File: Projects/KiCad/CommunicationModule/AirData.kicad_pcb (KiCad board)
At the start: 2 copper layers, 110 x 95 mm, 36 parts, among them J1 Conn_01x08, SW1 SW_DIP_x02, U1 MCP2562-E-P, U2 MCP2515-I/P, U3 NJM7805SDL1, U4 ABX00012, Y1 8MHz

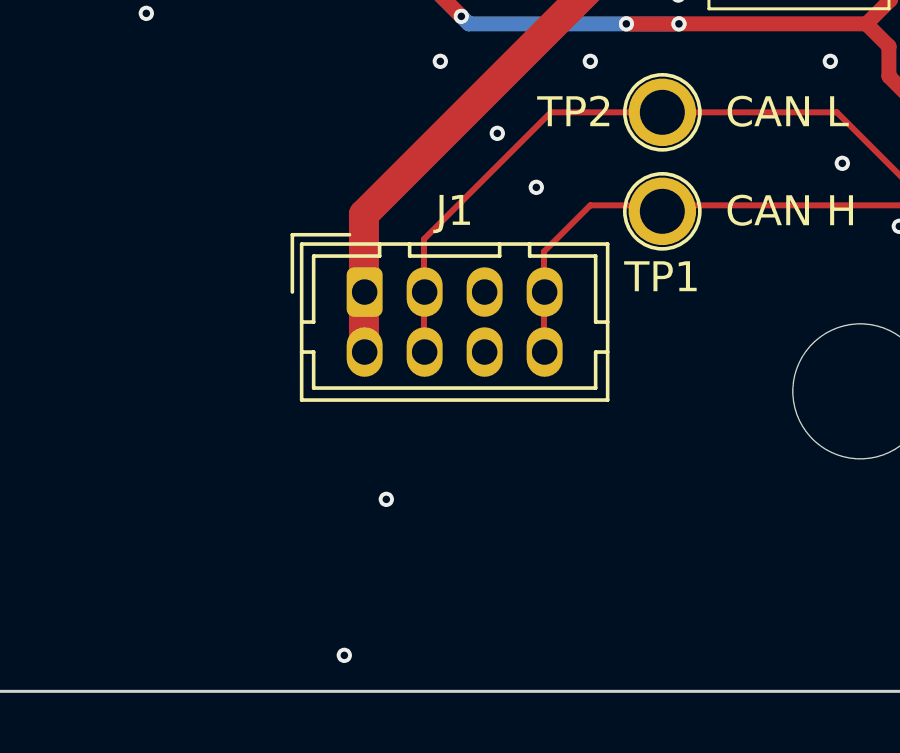
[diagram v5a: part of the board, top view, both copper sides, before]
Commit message: STEPファイルを再生成
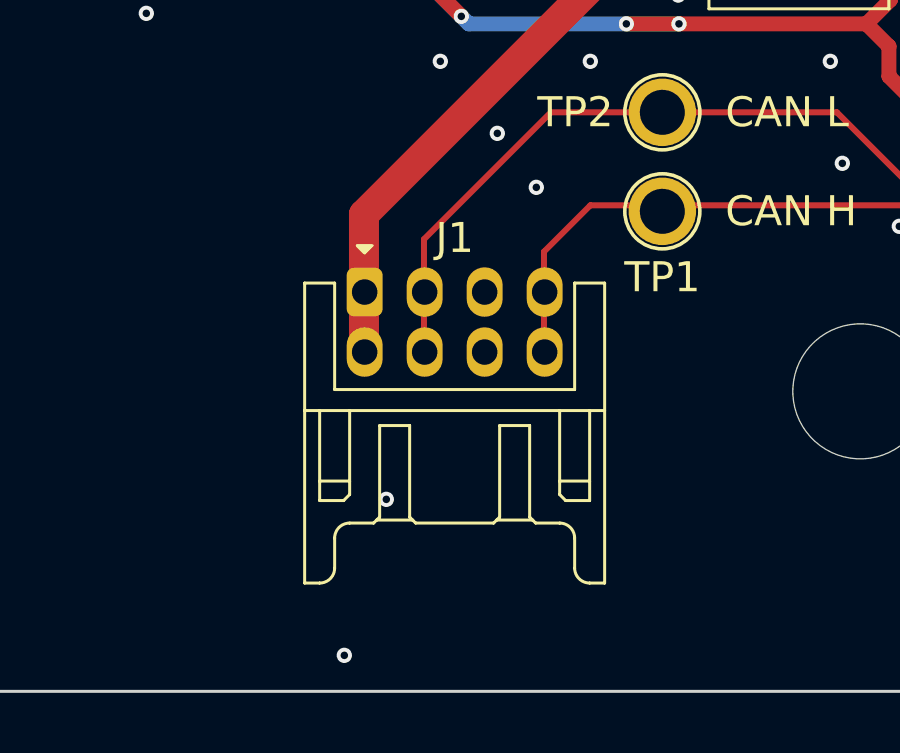
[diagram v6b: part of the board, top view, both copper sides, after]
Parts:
- J1: footprint Connector_Hirose:Hirose_DF11-8DP-2DSA_2x04_P2.00mm_Vertical -> Hirose_Connector:Hirose_DF11B-8DP-2DS
